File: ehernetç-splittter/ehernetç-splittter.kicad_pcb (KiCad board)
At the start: 2 copper layers, 73.7 x 27.9 mm, 7 parts, among them J1 RJ_can, J2 RJ_can, J3 RJ_can, J4 RJ_can

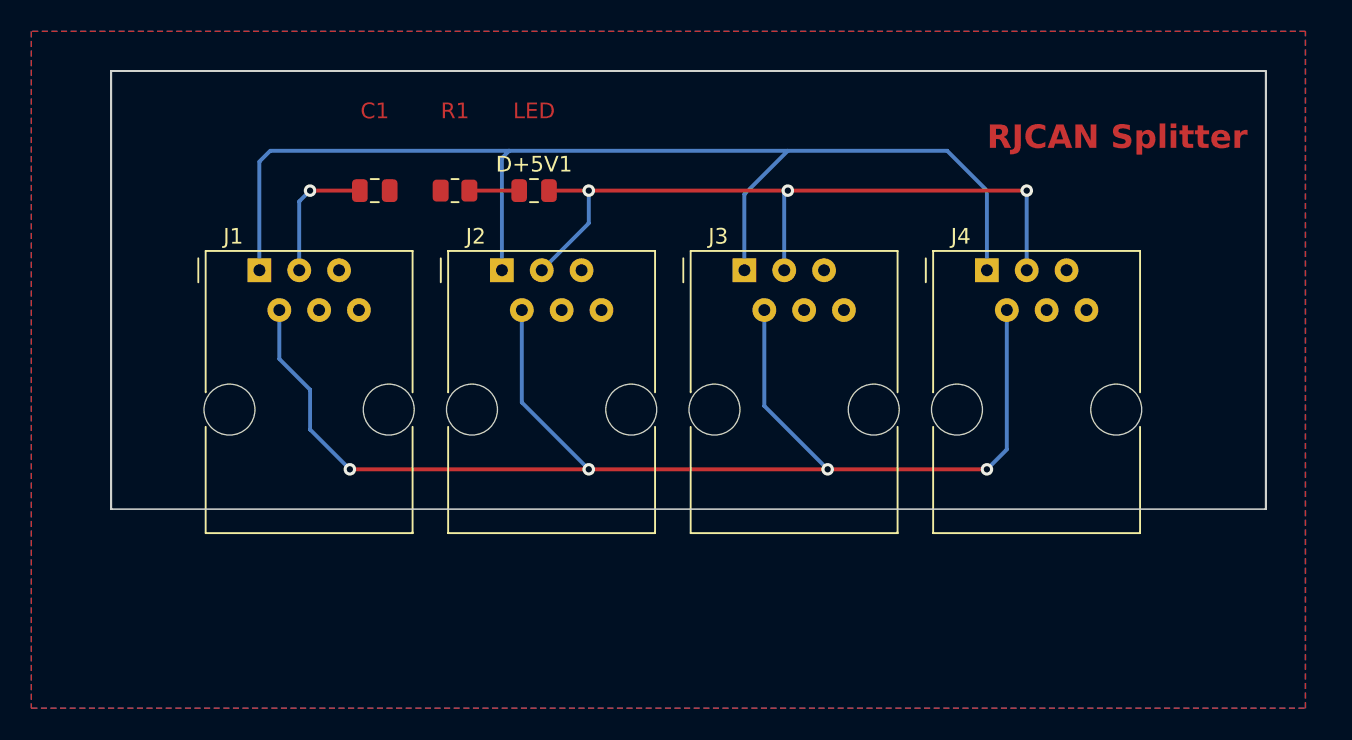
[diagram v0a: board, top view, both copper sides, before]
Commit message: added some vias for the grownd plain
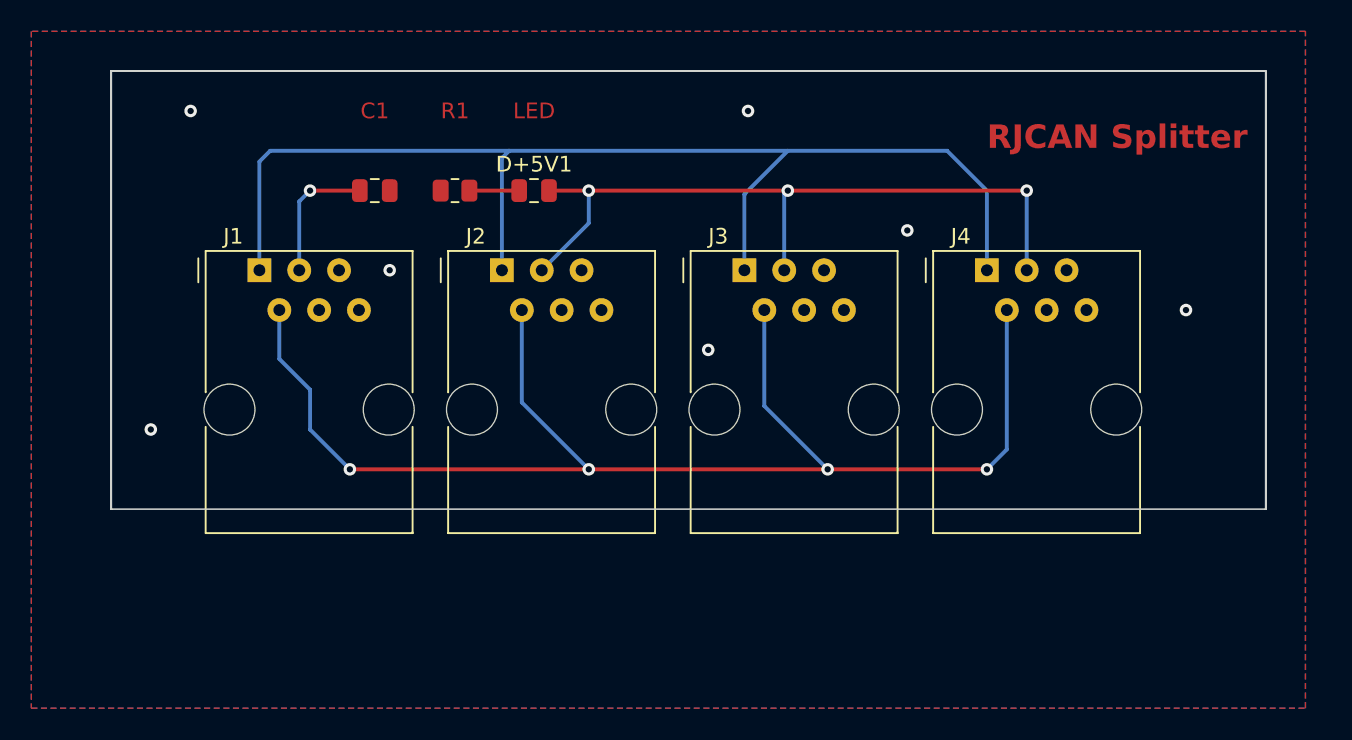
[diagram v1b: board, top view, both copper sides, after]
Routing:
- net GND: vias 0 -> 7
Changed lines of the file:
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@@
     (pad_to_mask_clearance 0)
     (pcbplotparams
-      (layerselection 0x00010fc_ffffffff)
+      (layerselection 0x0001000_ffffffff)
       (plot_on_all_layers_selection 0x0000000_00000000)
       (disableapertmacros false)
@@
       (outputformat 1)
       (mirror false)
-      (drillshape 1)
+      (drillshape 0)
       (scaleselection 1)
-      (outputdirectory "")
+      (outputdirectory "../fab/")
     )
   )
@@
   (segment (start 129.31 71.35) (end 129.54 71.12) (width 0.25) (layer "B.Cu") (net 1))
   (segment (start 98.37 71.81) (end 99.06 71.12) (width 0.25) (layer "B.Cu") (net 1))
+  (via (at 88.9 86.36) (size 0.8) (drill 0.4) (layers "F.Cu" "B.Cu") (free) (net 2))
+  (via (at 154.94 78.74) (size 0.8) (drill 0.4) (layers "F.Cu" "B.Cu") (free) (net 2))
+  (via (at 127 66.04) (size 0.8) (drill 0.4) (layers "F.Cu" "B.Cu") (free) (net 2))
+  (via (at 91.44 66.04) (size 0.8) (drill 0.4) (layers "F.Cu" "B.Cu") (free) (net 2))
+  (via (at 104.14 76.2) (size 0.8) (drill 0.4) (layers "F.Cu" "B.Cu") (free) (net 2))
+  (via (at 124.46 81.28) (size 0.8) (drill 0.4) (layers "F.Cu" "B.Cu") (free) (net 2))
+  (via (at 137.16 73.66) (size 0.8) (drill 0.4) (layers "F.Cu" "B.Cu") (free) (net 2))
   (segment (start 112.4 71.12) (end 109.22 71.12) (width 0.25) (layer "F.Cu") (net 3))
   (segment (start 111.3 76.2) (end 111.3 69.04) (width 0.25) (layer "B.Cu") (net 4))
